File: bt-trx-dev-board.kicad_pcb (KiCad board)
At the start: 2 copper layers, 78 x 68 mm, 51 parts, among them J1 RJ45, J2 PTT_BUTTON, J3 AudioJack2, J4 ENABLE_PTT_IN, J5 PTT_SELECT, J6 I2C, SW1 SW_Push, U1 SILabs_WT32i, U3 ESP32-DEVKITC-32D

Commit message: [#1] Deratsnested PCB
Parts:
- added C8: 15pF, Capacitor_SMD:C_0805_2012Metric_Pad1.15x1.40mm_HandSolder, F.Cu at (157.3, 83.7)
- added JP2: BYPASS, Jumper:SolderJumper-2_P1.3mm_Open_TrianglePad1.0x1.5mm, F.Cu at (163.7, 74.0)
- added L5: 100nH, Inductor_SMD:L_0805_2012Metric_Pad1.15x1.40mm_HandSolder, F.Cu at (162.9, 77.9)
- C5, C6: value 10nF -> 15pF
- J4: value ENABLE_PTT_IN -> ENAPLE_PTT_PULLUP
- SW1: footprint Button_Switch_THT:SW_Tactile_SKHH_Angled -> Button_Switch_SMD:Panasonic_EVQPUL_EVQPUC
- moved SW1 71.5 mm to (196.0, 110.5), turned to 270 degrees
- moved R2 65.2 mm to (191.6, 107.8)
- moved L3 2.85 mm to (174.2, 78.7)
- moved C2 2.28 mm to (158.2, 80.3)
- moved TP7 2.11 mm to (177.8, 79.4)
- moved C5 1.81 mm to (160.9, 77.9)
- moved C3 1.41 mm to (158.1, 76.8)
- moved D1 1.33 mm to (196.7, 94.1)
- moved D5 1.11 mm to (196.8, 103.5)
- moved D4 0.94 mm to (196.8, 99.0)
- moved TP1 0.57 mm to (177.8, 84.3)
- moved L1 0.50 mm to (174.1, 84.3)
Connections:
- C2 pad 1: GND -> AUDIO_B
- C3 pad 1: AUDIO_B -> Net-(C3-Pad1)
- C5 pad 1: AUDIO_B -> Net-(C3-Pad1)
- J1 pad 1: (no net) -> /CAT_TX
- J1 pad 3: (no net) -> /CAT_RX
- J4 pad 2: /UC_PTT_IN -> Net-(J4-Pad2)
- R1 pad 2: /UC_PTT_IN -> Net-(J4-Pad2)
- SW1 pad 1: /Microcontroller/BTN0 -> GND
- SW1 pad 2: GND -> /Microcontroller/BTN0
- U1 pad 20: /UART_UC_CTS -> (no net)
- U1 pad 21: /UART_UC_RTS -> (no net)
- U3 pad 12: (no net) -> /CAT_TX
- U3 pad 13: (no net) -> /CAT_RX
- U3 pad 28: /UART_UC_CTS -> (no net)
- U3 pad 29: /UART_UC_RTS -> (no net)
- U3 pad 7: /UC_PTT_IN -> /PTT_BUTTON

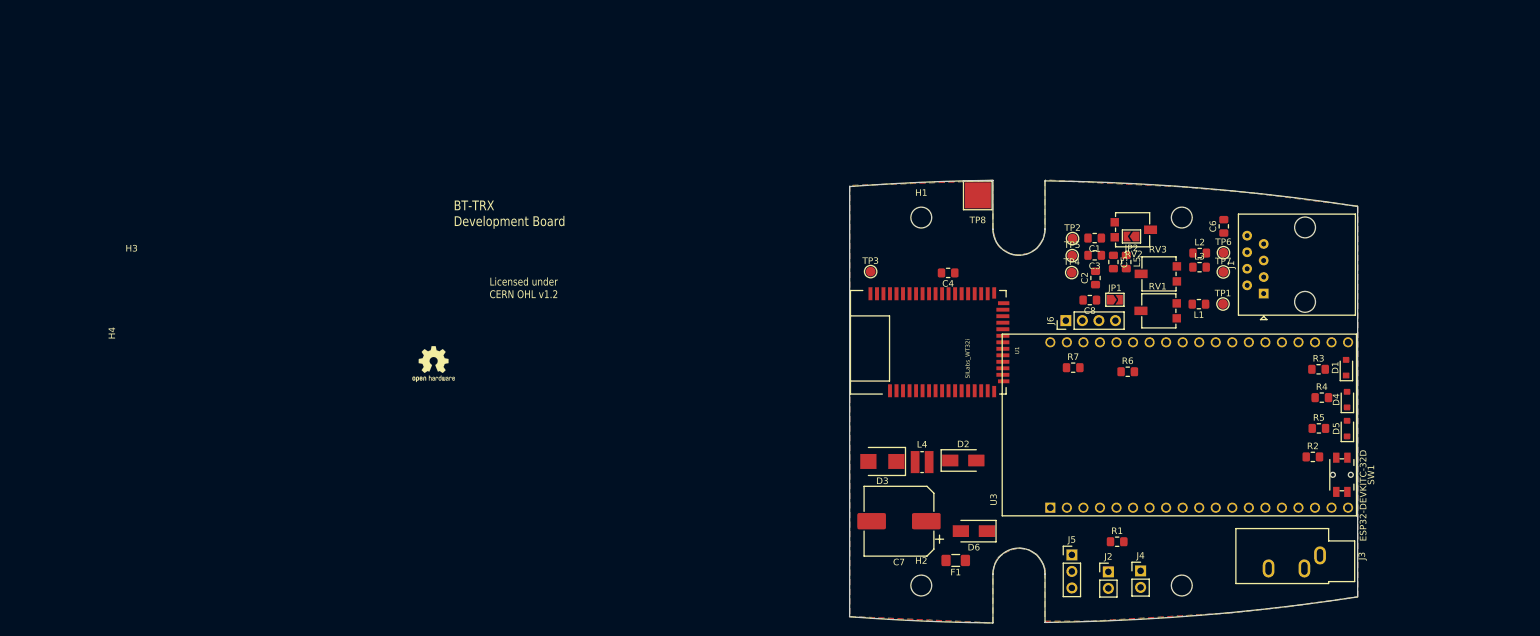
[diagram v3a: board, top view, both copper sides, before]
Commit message: [#1] Continued PCB
* Moved button pin for better tracability
* Added all missing traces
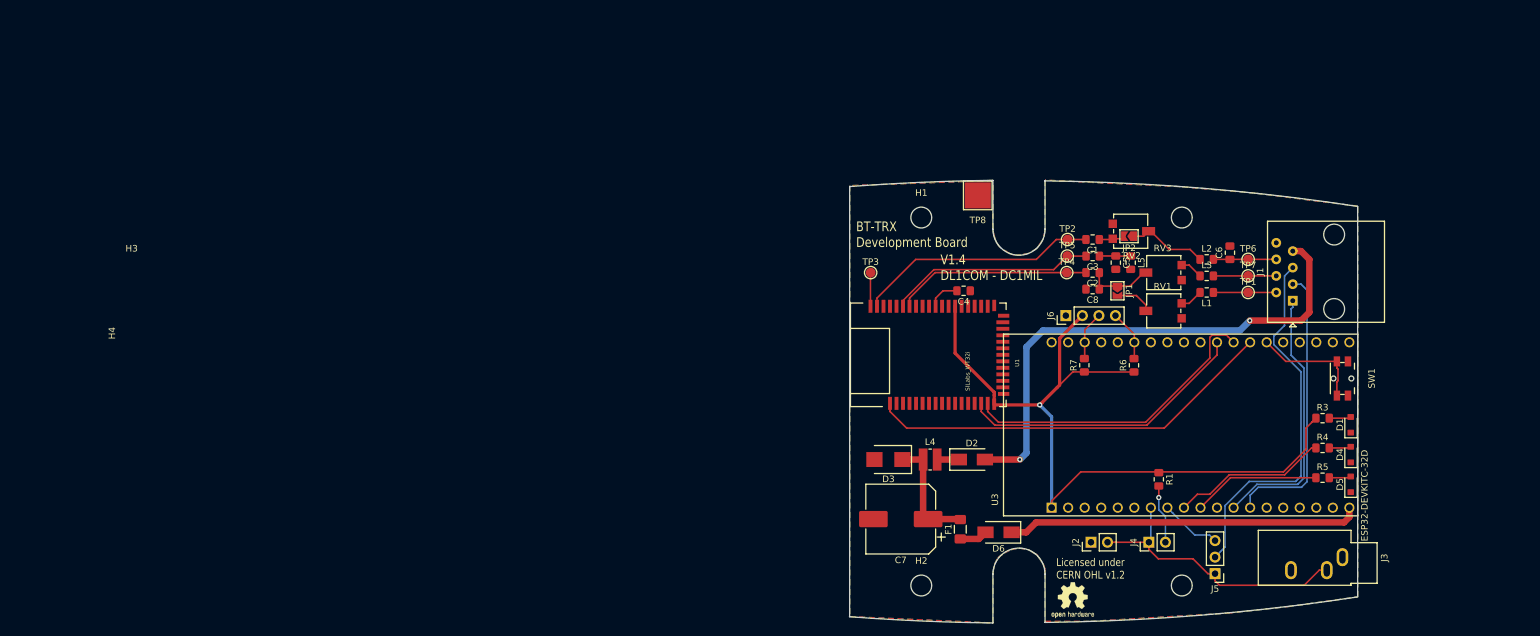
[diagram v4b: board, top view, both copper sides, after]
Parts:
- removed R2: 10k, Resistor_SMD:R_0805_2012Metric_Pad1.15x1.40mm_HandSolder
- moved N1 104.6 mm to (154.7, 129.8)
- moved J5 22.2 mm to (176.5, 125.7), turned to 180 degrees
- moved SW1 14.8 mm to (196.1, 95.8)
- moved R1 11.5 mm to (167.9, 111.2), turned to 270 degrees
- moved D1 8.80 mm to (197.4, 102.9)
- moved D5 8.58 mm to (197.4, 112.0)
- moved D4 8.46 mm to (197.4, 107.4)
- moved R4 7.73 mm to (193.0, 106.4)
- moved R5 7.59 mm to (193.0, 111.0)
- moved R3 7.53 mm to (193.0, 101.9)
- moved J2 5.27 mm to (157.5, 120.9), turned to 90 degrees
- moved F1 4.84 mm to (137.4, 118.9), turned to 90 degrees
- moved J1 4.60 mm to (188.5, 83.8)
- moved J4 4.58 mm to (166.4, 120.9), turned to 90 degrees
- moved TP1 4.25 mm to (181.6, 82.5)
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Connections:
- U3 pad 21: /WT32_ONOFF_FROM_UC -> (no net)
- U3 pad 32: /Microcontroller/BTN0 -> /WT32_ONOFF_FROM_UC
- U3 pad 33: (no net) -> /Microcontroller/BTN0
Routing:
- net +3V3: track 0.00 -> 119.1 mm, vias 0 -> 1
- net /V_IN: track 0.00 -> 79.9 mm, vias 0 -> 2
- net /WT32_ONOFF_FROM_UC: track 0.00 -> 63.1 mm
- net /PTT: track 0.00 -> 57.0 mm
- net +5V: track 0.00 -> 54.3 mm
- net /UART_UC_RX: track 0.00 -> 47.6 mm
- net /UART_UC_TX: track 0.00 -> 44.8 mm
- net /PTT_BUTTON: track 0.00 -> 44.1 mm
- net /CAT_RX: track 0.00 -> 43.5 mm
- net /CAT_TX: track 0.00 -> 40.9 mm
- net /SPK_LN: track 0.00 -> 37.1 mm
- net /MIC_LN: track 0.00 -> 31.8 mm
- net /MIC_LP: track 0.00 -> 30.0 mm
- net /Microcontroller/LED0: track 0.00 -> 24.1 mm
- net /Microcontroller/LED1: track 0.00 -> 19.6 mm
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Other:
- board text added: "V1.4 DL1COM - DC1MIL"

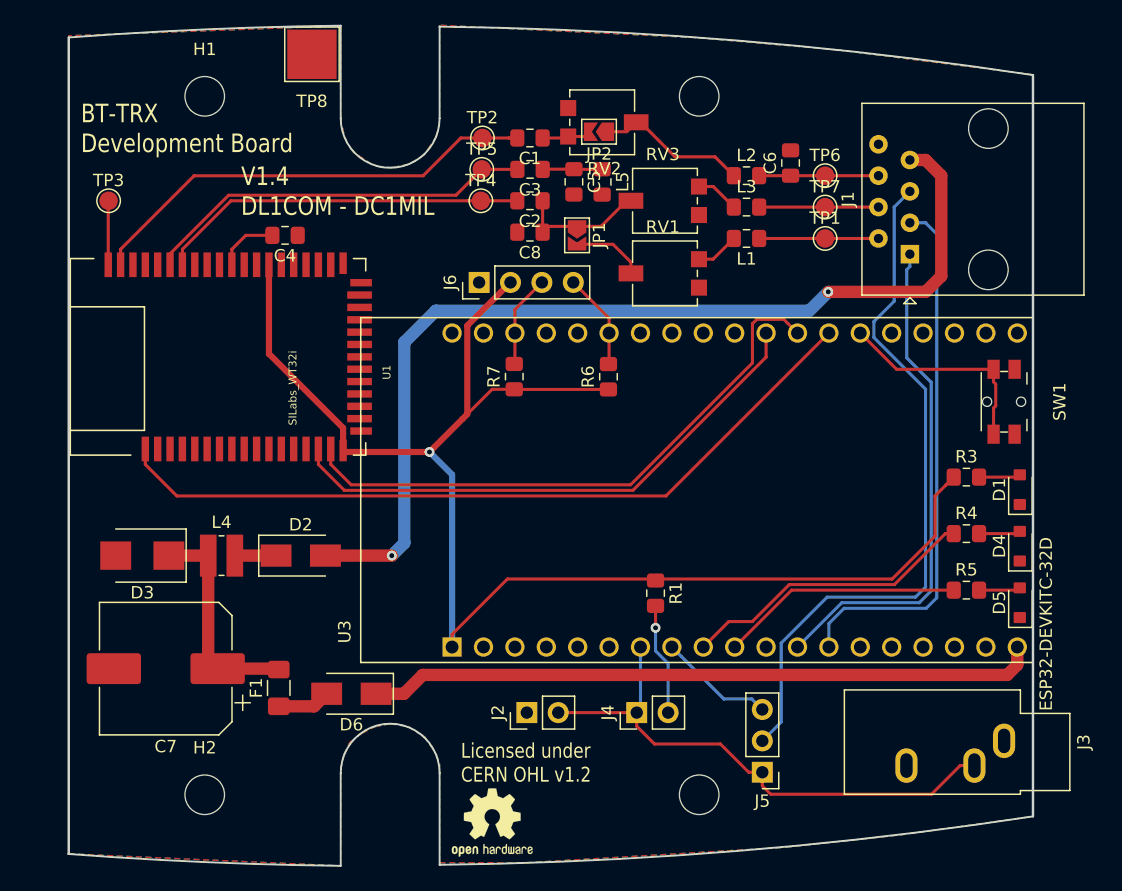
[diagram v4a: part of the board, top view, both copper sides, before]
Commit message: [#2] Beatufied PCB
* Put all silkscreen items on the right place
* Added keepout to BT antenna
* Added couple of vias for better grounding
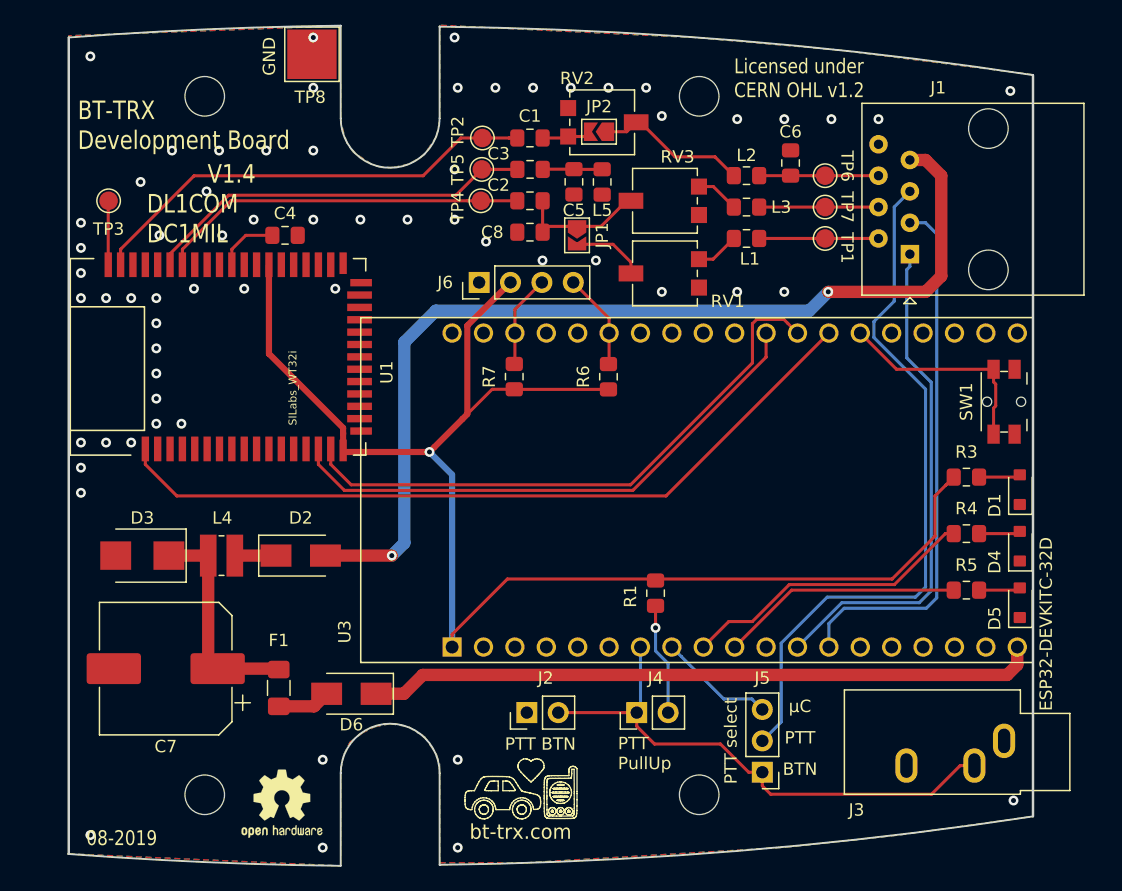
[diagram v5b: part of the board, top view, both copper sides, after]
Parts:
- moved N1 17.1 mm to (137.7, 128.3)
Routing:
- net GND: vias 0 -> 63
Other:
- board text added: "08-2019"
- board text added: "BTN"
- board text added: "GND"
- board text added: "PTT"
- board text added: "PTT BTN"
- board text added: "PTT PullUp"
- board text added: "PTT select"
- board text added: "V1.4 DL1COM DC1MIL"
- board text added: "bt-trx.com"
- board text added: "µC"
- board text removed: "V1.4 DL1COM - DC1MIL"
